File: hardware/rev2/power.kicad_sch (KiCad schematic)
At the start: 22 parts, among them J8 Battery Connection, U5 MP2664GG-xxxx-P, U6 MAX17055ETB+, U8 TPS631000DRLR

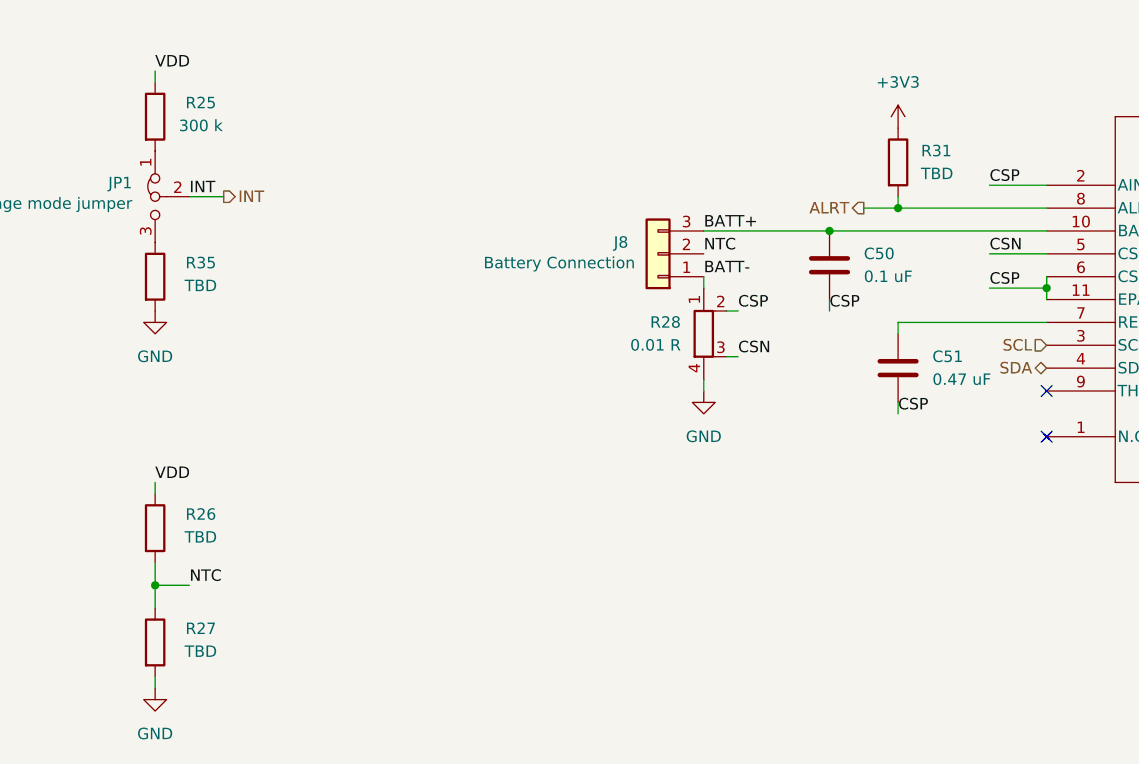
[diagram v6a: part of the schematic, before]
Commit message: Added part number for power system passive components
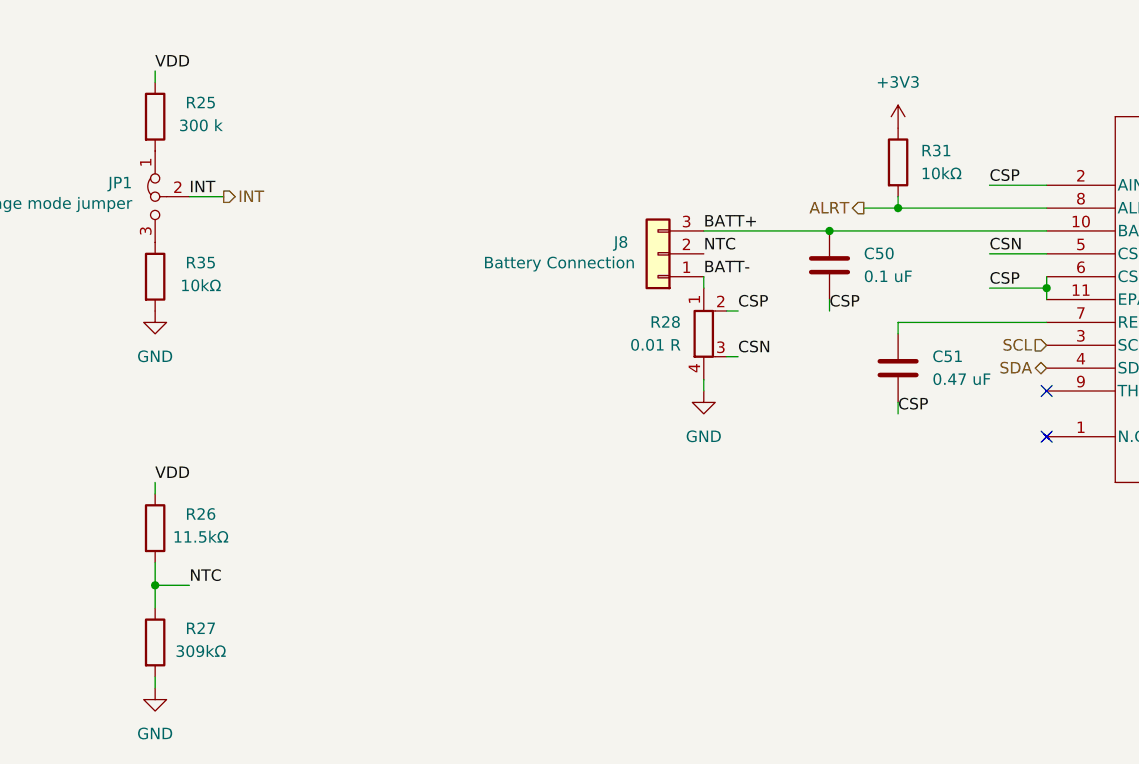
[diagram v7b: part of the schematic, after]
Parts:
- C48: Mouser Part Number (none) -> 81-GCJ188R71E104KA2D
- C49: Mouser Part Number (none) -> 81-GRM188Z71A475KE5D
- C51: Mouser Part Number (none) -> 187-CL10B474KP8NNNC
- J8: Mouser Part Number (none) -> 538-53047-0310
- R25: Mouser Part Number (none) -> 603-AC0603FR-07300KL
- R26: value TBD -> 11.5kΩ; Mouser Part Number (none) -> 667-ERA-3AEB1152V
- R27: value TBD -> 309kΩ; Mouser Part Number (none) -> 667-ERA-3AEB3093V
- R29: Mouser Part Number (none) -> 708-RMCF0603FT511K
- R30: Mouser Part Number (none) -> 708-RMCF0603FT91K0
- R31, R35: value TBD -> 10kΩ; Mouser Part Number (none) -> 71-CRCW060310K0JNEAC
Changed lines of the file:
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@@
 			)
 		)
-		(property "Value" "TBD"
+		(property "Value" "10kΩ"
 			(at 43.18 130.556 0)
 			(show_name no)
@@
 			)
 		)
-		(property "Datasheet" ""
+		(property "Datasheet" "https://www.vishay.com/docs/20035/dcrcwe3.pdf"
 			(at 38.1 129.54 0)
 			(hide yes)
@@
 		)
 		(property "Sim.Type" ""
+			(at 38.1 129.54 0)
+			(hide yes)
+			(show_name no)
+			(do_not_autoplace no)
+			(effects
+				(font
+					(size 1.27 1.27)
+				)
+			)
+		)
+		(property "Mouser Part Number" "71-CRCW060310K0JNEAC"
 			(at 38.1 129.54 0)
 			(hide yes)
@@
 			)
 		)
-		(property "Value" "TBD"
+		(property "Value" "11.5kΩ"
 			(at 43.18 158.496 0)
 			(show_name no)
@@
 			)
 		)
-		(property "Datasheet" ""
+		(property "Datasheet" "https://industrial.panasonic.com/cdbs/www-data/pdf/RDM0000/AOA0000C307.pdf"
 			(at 38.1 157.48 0)
 			(hide yes)
@@
 		)
 		(property "Sim.Type" ""
+			(at 38.1 157.48 0)
+			(hide yes)
+			(show_name no)
+			(do_not_autoplace no)
+			(effects
+				(font
+					(size 1.27 1.27)
+				)
+			)
+		)
+		(property "Mouser Part Number" "667-ERA-3AEB1152V"
 			(at 38.1 157.48 0)
 			(hide yes)
@@
 			)
 		)
-		(property "Datasheet" ""
+		(property "Datasheet" "https://www.mouser.se/datasheet/3/1099/1/SEI_RMCF_RMCP.pdf"
 			(at 203.2 53.34 0)
 			(hide yes)
@@
 			)
 		)
+		(property "Mouser Part Number" "708-RMCF0603FT511K"
+			(at 203.2 53.34 0)
+			(hide yes)
+			(show_name no)
+			(do_not_autoplace no)
+			(effects
+				(font
+					(size 1.27 1.27)
+				)
+			)
+		)
 		(pin "2"
 		)
@@
 			)
 		)
-		(property "Datasheet" ""
+		(property "Datasheet" "https://weblib.samsungsem.com/mlcc/mlcc-ec-data-sheet.do?partNumber=CL10B474KP8NNN"
 			(at 120.65 139.7 0)
 			(hide yes)
@@
 		)
 		(property "Sim.Type" ""
+			(at 120.65 139.7 0)
+			(hide yes)
+			(show_name no)
+			(do_not_autoplace no)
+			(effects
+				(font
+					(size 1.27 1.27)
+				)
+			)
+		)
+		(property "Mouser Part Number" "187-CL10B474KP8NNNC"
 			(at 120.65 139.7 0)
 			(hide yes)
@@
 			)
 		)
-		(property "Datasheet" ""
+		(property "Datasheet" "https://www.mouser.se/datasheet/3/1099/1/SEI_RMCF_RMCP.pdf"
 			(at 203.2 60.96 0)
 			(hide yes)
@@
 		)
 		(property "Sim.Type" ""
+			(at 203.2 60.96 0)
+			(hide yes)
+			(show_name no)
+			(do_not_autoplace no)
+			(effects
+				(font
+					(size 1.27 1.27)
+				)
+			)
+		)
+		(property "Mouser Part Number" "708-RMCF0603FT91K0"
 			(at 203.2 60.96 0)
 			(hide yes)
@@
 			)
 		)
-		(property "Datasheet" ""
+		(property "Datasheet" "https://www.mouser.se/datasheet/3/76/1/GCJ188R71E104KA12_02B.pdf"
 			(at 52.07 86.36 0)
 			(hide yes)
@@
 		)
 		(property "Sim.Type" ""
+			(at 52.07 86.36 0)
+			(hide yes)
+			(show_name no)
+			(do_not_autoplace no)
+			(effects
+				(font
+					(size 1.27 1.27)
+				)
+			)
+		)
+		(property "Mouser Part Number" "81-GCJ188R71E104KA2D"
 			(at 52.07 86.36 0)
 			(hide yes)
@@
 			)
 		)
-		(property "Datasheet" ""
+		(property "Datasheet" "https://pim.murata.com/asset/pim4/ceramicCapacitorSMD/GRM188Z71A475KE15-01A-EN_PDF_CERAMICCAPACITORSMD"
 			(at 115.57 82.55 0)
 			(hide yes)
@@
 		)
 		(property "Sim.Type" ""
+			(at 115.57 82.55 0)
+			(hide yes)
+			(show_name no)
+			(do_not_autoplace no)
+			(effects
+				(font
+					(size 1.27 1.27)
+				)
+			)
+		)
+		(property "Mouser Part Number" "81-GRM188Z71A475KE5D"
 			(at 115.57 82.55 0)
 			(hide yes)
@@
 			)
 		)
-		(property "Datasheet" ""
+		(property "Datasheet" "https://www.molex.com/en-us/products/part-detail-pdf/530470310?display=pdf"
 			(at 93.98 127 0)
 			(hide yes)
@@
 			)
 		)
+		(property "Mouser Part Number" "538-53047-0310"
+			(at 93.98 127 0)
+			(hide yes)
+			(show_name no)
+			(do_not_autoplace no)
+			(effects
+				(font
+					(size 1.27 1.27)
+				)
+			)
+		)
 		(pin "1"
 		)
@@
 			)
 		)
-		(property "Datasheet" ""
+		(property "Datasheet" "https://www.mouser.se/datasheet/3/508/1/PYU_AC_51_ROHS_L.pdf"
 			(at 38.1 111.76 0)
 			(hide yes)
@@
 		)
 		(property "Sim.Type" ""
+			(at 38.1 111.76 0)
+			(hide yes)
+			(show_name no)
+			(do_not_autoplace no)
+			(effects
+				(font
+					(size 1.27 1.27)
+				)
+			)
+		)
+		(property "Mouser Part Number" "603-AC0603FR-07300KL"
 			(at 38.1 111.76 0)
 			(hide yes)
@@
 			)
 		)
-		(property "Value" "TBD"
+		(property "Value" "309kΩ"
 			(at 43.18 171.196 0)
 			(show_name no)
@@
 			)
 		)
-		(property "Datasheet" ""
+		(property "Datasheet" "https://industrial.panasonic.com/cdbs/www-data/pdf/RDM0000/AOA0000C307.pdf"
 			(at 38.1 170.18 0)
 			(hide yes)
@@
 		)
 		(property "Sim.Type" ""
+			(at 38.1 170.18 0)
+			(hide yes)
+			(show_name no)
+			(do_not_autoplace no)
+			(effects
+				(font
+					(size 1.27 1.27)
+				)
+			)
+		)
+		(property "Mouser Part Number" "667-ERA-3AEB3093V"
 			(at 38.1 170.18 0)
 			(hide yes)
@@
 			)
 		)
-		(property "Value" "TBD"
+		(property "Value" "10kΩ"
 			(at 123.19 118.11 0)
 			(show_name no)
@@
 			)
 		)
-		(property "Datasheet" ""
+		(property "Datasheet" "https://www.vishay.com/docs/20035/dcrcwe3.pdf"
 			(at 120.65 116.84 0)
 			(hide yes)
@@
 			(at 120.65 116.84 0)
 			(hide yes)
+			(show_name no)
+			(do_not_autoplace no)
+			(effects
+				(font
+					(size 1.27 1.27)
+				)
+			)
+		)
+		(property "Mouser Part Number" "71-CRCW060310K0JNEAC"
+			(at 120.65 116.84 0)
+			(hide yes)

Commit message: Replaced charger wake-up cap jumper headers
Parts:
- JP1: footprint Connector_PinHeader_1.00mm:PinHeader_1x03_P1.00mm_Vertical -> Connector_PinHeader_1.27mm:PinHeader_1x03_P1.27mm_Vertical_SMD_Pin1Right; Mouser Part Number (none) -> 200-FTR10302SS and 855-M50-1900005; now in the parts list
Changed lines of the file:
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@@
 		(body_style 1)
 		(exclude_from_sim no)
-		(in_bom no)
+		(in_bom yes)
 		(on_board yes)
 		(in_pos_files yes)
@@
 			)
 		)
-		(property "Footprint" "Connector_PinHeader_1.00mm:PinHeader_1x03_P1.00mm_Vertical"
+		(property "Footprint" "Connector_PinHeader_1.27mm:PinHeader_1x03_P1.27mm_Vertical_SMD_Pin1Right"
 			(at 38.1 120.65 0)
 			(hide yes)
@@
 			)
 		)
-		(property "Datasheet" ""
+		(property "Datasheet" "https://www.mouser.se/datasheet/3/85/1/ftr_smt.pdf"
 			(at 38.1 120.65 0)
 			(hide yes)
@@
 			(hide yes)
 			(show_name no)
+			(do_not_autoplace no)
+			(effects
+				(font
+					(size 1.27 1.27)
+				)
+			)
+		)
+		(property "Mouser Part Number" "200-FTR10302SS and 855-M50-1900005"
+			(at 38.1 120.65 90)
+			(hide yes)
+			(show_name no)
